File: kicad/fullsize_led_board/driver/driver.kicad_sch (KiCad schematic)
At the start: 131 parts, among them J4 Anodes Header, J5 Cathodes Header, Q1 SQ2351CES, Q10 SQ2351CES, Q11 SQ2351CES, Q12 SQ2351CES, Q13 SQ2351CES, Q14 SQ2351CES, Q15 SQ2351CES, Q16 SQ2351CES, Q17 SQ2351CES, Q18 SQ2351CES, Q19 SQ2351CES, Q2 SQ2351CES, Q20 SQ2351CES, Q21 SQ2351CES, Q22 SQ2351CES, Q23 SQ2351CES, Q24 SQ2351CES, Q3 SQ2351CES, Q4 SQ2351CES, Q5 SQ2351CES, Q6 SQ2351CES, Q7 SQ2351CES, Q8 SQ2351CES, Q9 SQ2351CES, U1 74HCT541, U2 74HCT595, U3 74HCT595, U4 74HCT595, U5 TPIC6B595N, U6 TPIC6B595N, U7 TPIC6B595N, U8 TPIC6B595N

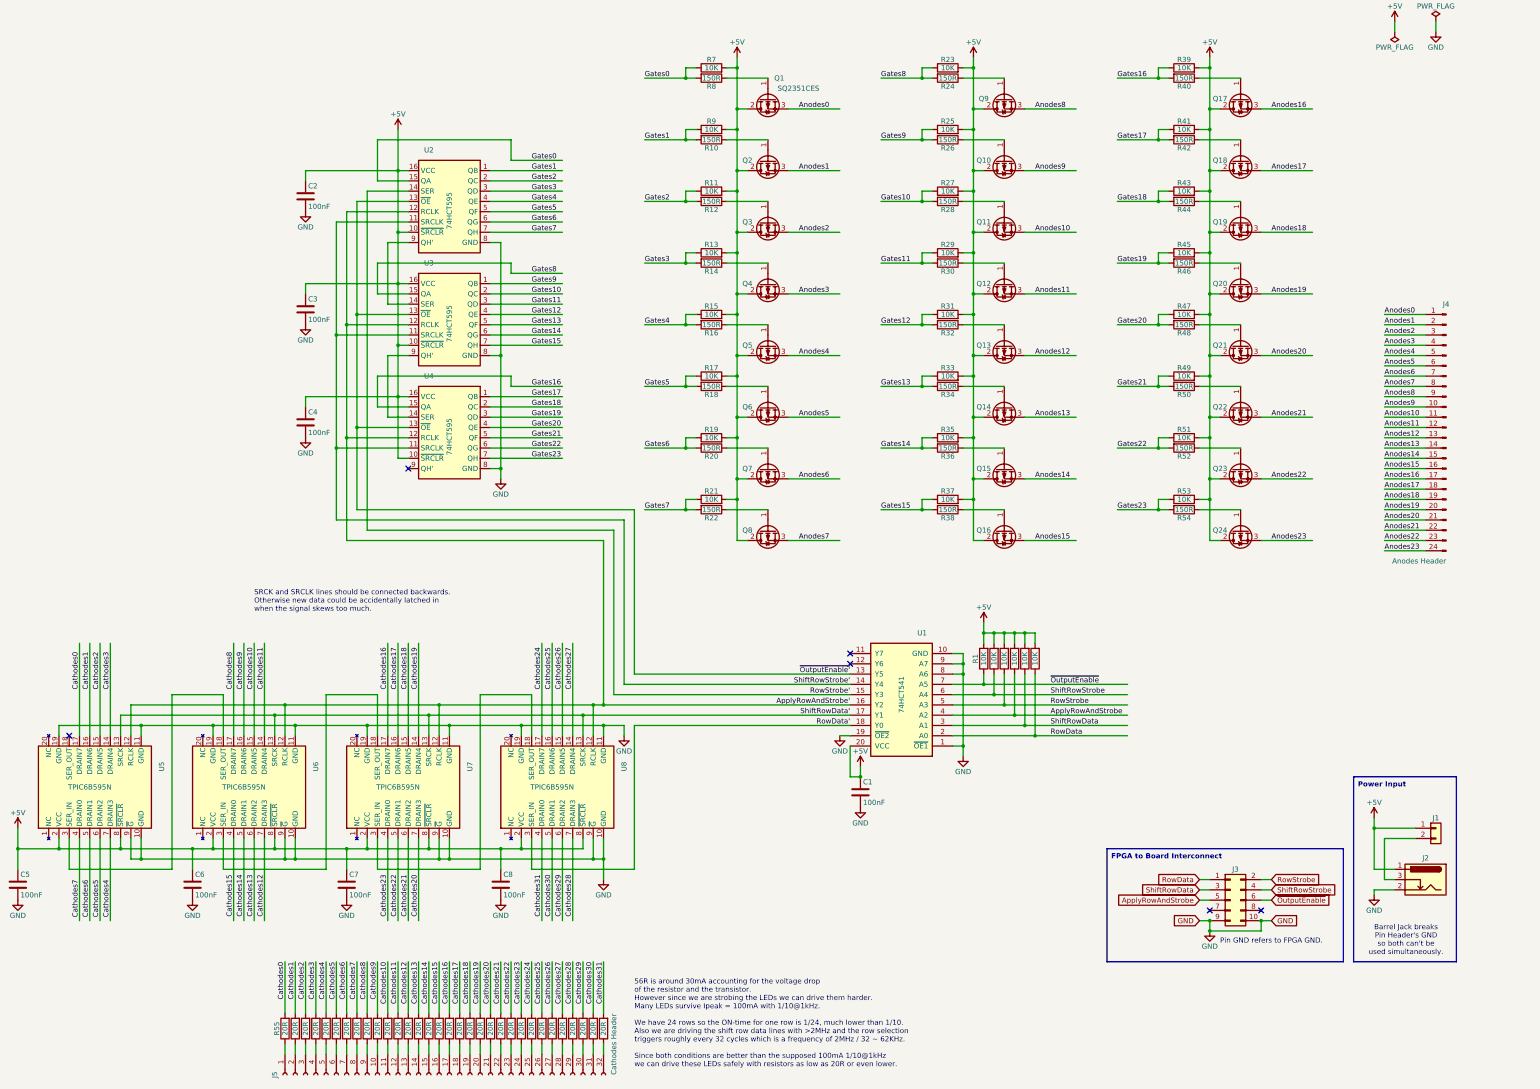
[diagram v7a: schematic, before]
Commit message: kicad: wip migrating to kicad 9.0, fullsize board done
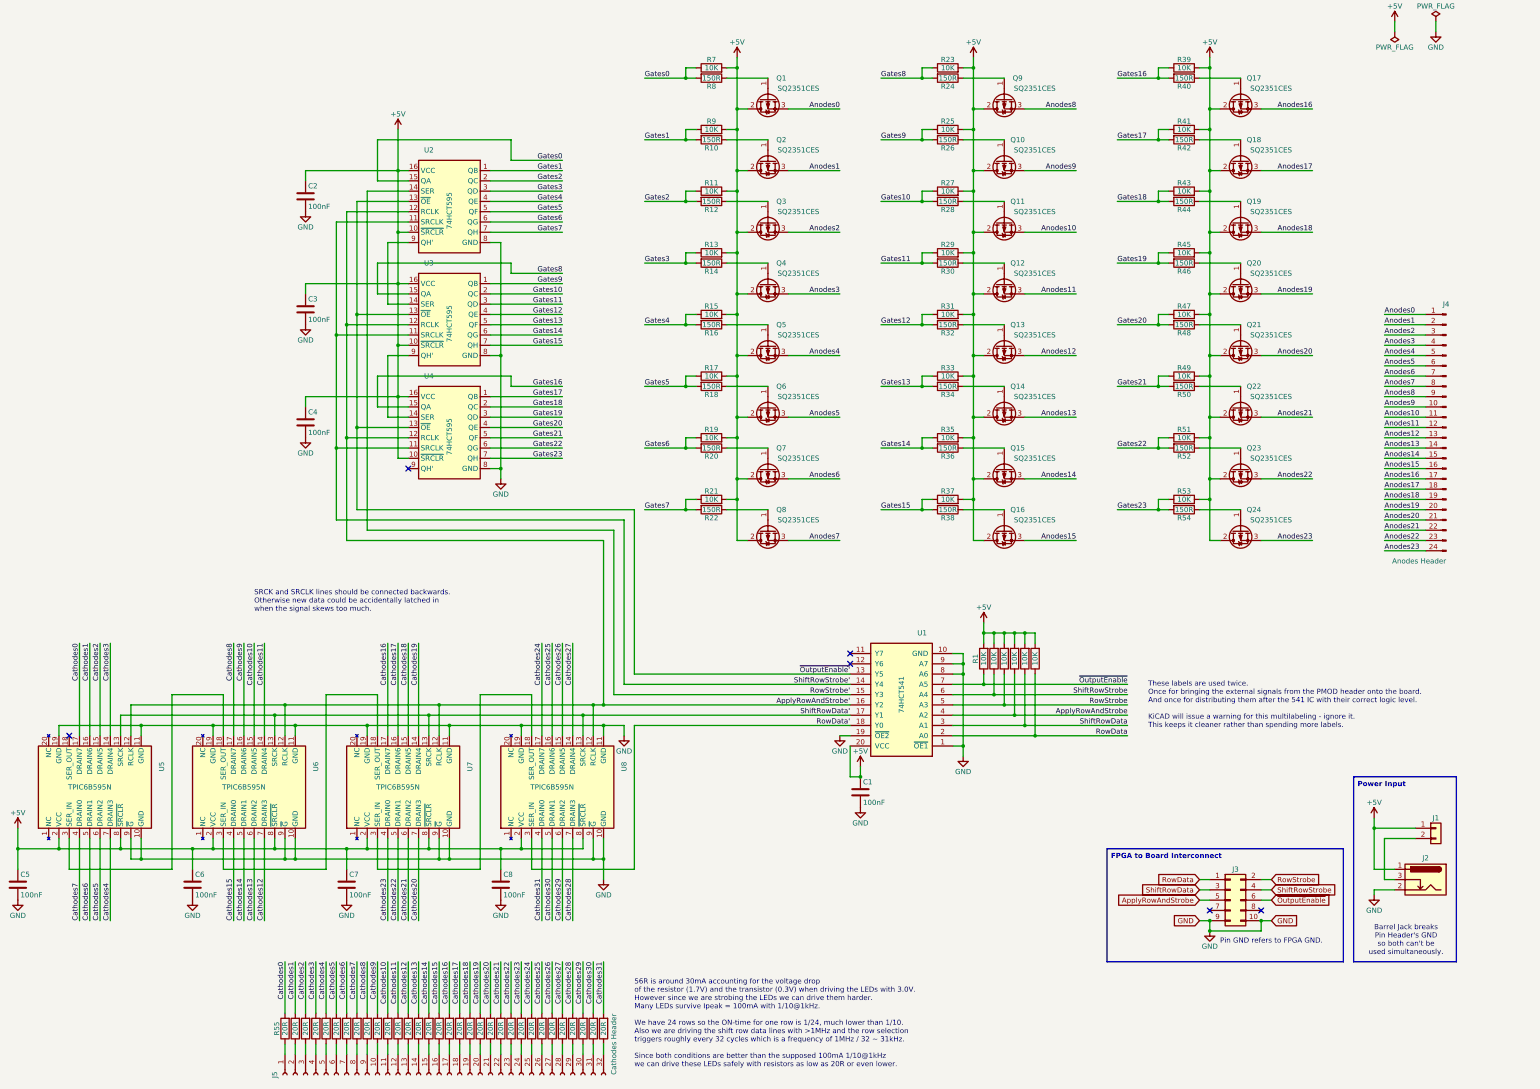
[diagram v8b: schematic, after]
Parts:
- removed Q1, Q10, Q11, Q12, Q13, Q14, Q15, Q16, Q17, Q18, Q19, Q2, Q20, Q21, Q22, Q23, Q24, Q3, Q4, Q5, Q6, Q7, Q8, Q9: SQ2351CES, Package_TO_SOT_SMD:SOT-23-3, symbol Transistor_FET:IRF4905
- removed U1: 74HCT541, Package_DIP:DIP-20_W7.62mm, symbol 74xx:74AHCT541
- removed U2, U3, U4: 74HCT595, Package_SO:SOIC-16_3.9x9.9mm_P1.27mm, symbol 74xx:74HCT595
- removed U5, U6, U7, U8: TPIC6B595N, Package_DIP:DIP-20_W7.62mm, symbol Interface_Expansion:TPIC6595
- added Q1, Q10, Q11, Q12, Q13, Q14, Q15, Q16, Q17, Q18, Q19, Q2, Q20, Q21, Q22, Q23, Q24, Q3, Q4, Q5, Q6, Q7, Q8, Q9: SQ2351CES, Package_TO_SOT_SMD:SOT-23-3, symbol symbol_library:SQ2351CES
- added U1: 74HCT541, Package_DIP:DIP-20_W7.62mm, symbol symbol_library:74HCT541
- added U2, U3, U4: 74HCT595, Package_SO:SOIC-16_3.9x9.9mm_P1.27mm, symbol symbol_library:74HCT595
- added U5, U6, U7, U8: TPIC6B595N, Package_DIP:DIP-20_W7.62mm, symbol symbol_library:TPIC6B595N
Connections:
- net +5V: now also Q1.2 (S), Q10.2 (S), Q11.2 (S), Q12.2 (S), Q13.2 (S), Q14.2 (S), Q15.2 (S), Q16.2 (S), Q17.2 (S), Q18.2 (S), Q19.2 (S), Q2.2 (S), Q20.2 (S), Q21.2 (S), Q22.2 (S), Q23.2 (S), Q24.2 (S), Q3.2 (S), Q4.2 (S), Q5.2 (S), Q6.2 (S), Q7.2 (S), Q8.2 (S), Q9.2 (S), U1.20 (VCC), U2.10 (~{SRCLR}), U2.16 (VCC), U3.10 (~{SRCLR}), U3.16 (VCC), U4.10 (~{SRCLR}), U4.16 (VCC), U5.2 (VCC), U5.8 (~{SRCLR}), U6.2 (VCC), U6.8 (~{SRCLR}), U7.2 (VCC), U7.8 (~{SRCLR}), U8.2 (VCC), U8.8 (~{SRCLR})
- net Anodes0: now also Q1.3 (D)
- net Anodes1: now also Q2.3 (D)
- net Anodes10: now also Q11.3 (D)
- net Anodes11: now also Q12.3 (D)
- net Anodes12: now also Q13.3 (D)
- net Anodes13: now also Q14.3 (D)
- net Anodes14: now also Q15.3 (D)
- net Anodes15: now also Q16.3 (D)
- net Anodes16: now also Q17.3 (D)
- net Anodes17: now also Q18.3 (D)
- net Anodes18: now also Q19.3 (D)
- net Anodes19: now also Q20.3 (D)
- net Anodes2: now also Q3.3 (D)
- net Anodes20: now also Q21.3 (D)
- net Anodes21: now also Q22.3 (D)
- net Anodes22: now also Q23.3 (D)
- net Anodes23: now also Q24.3 (D)
- net Anodes3: now also Q4.3 (D)
- net Anodes4: now also Q5.3 (D)
- net Anodes5: now also Q6.3 (D)
- net Anodes6: now also Q7.3 (D)
- net Anodes7: now also Q8.3 (D)
- net Anodes8: now also Q9.3 (D)
- net Anodes9: now also Q10.3 (D)
- net ApplyRowAndStrobe: now also U1.4 (A2)
- net ApplyRowAndStrobe': now also U1.16 (Y2), U2.12 (RCLK), U3.12 (RCLK), U4.12 (RCLK), U5.12 (RCLK), U6.12 (RCLK), U7.12 (RCLK), U8.12 (RCLK)
- net Cathodes0: now also U5.17 (DRAIN7)
- net Cathodes1: now also U5.16 (DRAIN6)
- net Cathodes10: now also U6.15 (DRAIN5)
- net Cathodes11: now also U6.14 (DRAIN4)
- net Cathodes12: now also U6.7 (DRAIN3)
- net Cathodes13: now also U6.6 (DRAIN2)
- net Cathodes14: now also U6.5 (DRAIN1)
- net Cathodes15: now also U6.4 (DRAIN0)
- net Cathodes16: now also U7.17 (DRAIN7)
- net Cathodes17: now also U7.16 (DRAIN6)
- net Cathodes18: now also U7.15 (DRAIN5)
- net Cathodes19: now also U7.14 (DRAIN4)
- net Cathodes2: now also U5.15 (DRAIN5)
- net Cathodes20: now also U7.7 (DRAIN3)
- net Cathodes21: now also U7.6 (DRAIN2)
- net Cathodes22: now also U7.5 (DRAIN1)
- net Cathodes23: now also U7.4 (DRAIN0)
- net Cathodes24: now also U8.17 (DRAIN7)
- net Cathodes25: now also U8.16 (DRAIN6)
- net Cathodes26: now also U8.15 (DRAIN5)
- net Cathodes27: now also U8.14 (DRAIN4)
- net Cathodes28: now also U8.7 (DRAIN3)
- net Cathodes29: now also U8.6 (DRAIN2)
- net Cathodes3: now also U5.14 (DRAIN4)
- net Cathodes30: now also U8.5 (DRAIN1)
- net Cathodes31: now also U8.4 (DRAIN0)
- net Cathodes4: now also U5.7 (DRAIN3)
- net Cathodes5: now also U5.6 (DRAIN2)
- net Cathodes6: now also U5.5 (DRAIN1)
- net Cathodes7: now also U5.4 (DRAIN0)
- net Cathodes8: now also U6.17 (DRAIN7)
- net Cathodes9: now also U6.16 (DRAIN6)
- net GND: now also U1.1 (~{OE1}), U1.10 (GND), U1.19 (~{OE2}), U1.8 (A6), U1.9 (A7), U2.8 (GND), U3.8 (GND), U4.8 (GND), U5.10 (GND), U5.11 (GND), U5.19 (GND), U5.9 (~{G}), U6.10 (GND), U6.11 (GND), U6.19 (GND), U6.9 (~{G}), U7.10 (GND), U7.11 (GND), U7.19 (GND), U7.9 (~{G}), U8.10 (GND), U8.11 (GND), U8.19 (GND), U8.9 (~{G})
- net Gates0: now also U2.15 (QA)
- net Gates1: now also U2.1 (QB)
- net Gates10: now also U3.2 (QC)
- net Gates11: now also U3.3 (QD)
- net Gates12: now also U3.4 (QE)
- net Gates13: now also U3.5 (QF)
- net Gates14: now also U3.6 (QG)
- net Gates15: now also U3.7 (QH)
- net Gates16: now also U4.15 (QA)
- net Gates17: now also U4.1 (QB)
- net Gates18: now also U4.2 (QC)
- net Gates19: now also U4.3 (QD)
- net Gates2: now also U2.2 (QC)
- net Gates20: now also U4.4 (QE)
- net Gates21: now also U4.5 (QF)
- net Gates22: now also U4.6 (QG)
- net Gates23: now also U4.7 (QH)
- net Gates3: now also U2.3 (QD)
- net Gates4: now also U2.4 (QE)
- net Gates5: now also U2.5 (QF)
- net Gates6: now also U2.6 (QG)
- net Gates7: now also U2.7 (QH)
- net Gates8: now also U3.15 (QA)
- net Gates9: now also U3.1 (QB)
- net RowData: now also U1.2 (A0)
- net RowData': now also U1.18 (Y0), U8.3 (SER_IN)
- net RowStrobe: now also U1.5 (A3)
- net RowStrobe': now also U1.15 (Y3), U2.14 (SER)
- net ShiftRowData: now also U1.3 (A1)
- net ShiftRowData': now also U1.17 (Y1), U5.13 (SRCK), U6.13 (SRCK), U7.13 (SRCK), U8.13 (SRCK)
- net ShiftRowStrobe: now also U1.6 (A4)
- net ShiftRowStrobe': now also U1.14 (Y4), U2.11 (SRCLK), U3.11 (SRCLK), U4.11 (SRCLK)
- net ~{OutputEnable'}: now also U1.13 (Y5), U2.13 (~{OE}), U3.13 (~{OE}), U4.13 (~{OE})
- net ~{OutputEnable}: now also U1.7 (A5)
- net at R26.1: now also Q10.1 (G)
- net at R48.1: now also Q21.1 (G)
- net at R50.1: now also Q22.1 (G)
- net at R32.1: now also Q13.1 (G)
- net at R12.1: now also Q3.1 (G)
- net at R46.1: now also Q20.1 (G)
- net at R34.1: now also Q14.1 (G)
- net at R40.1: now also Q17.1 (G)
- net at R30.1: now also Q12.1 (G)
- net at R42.1: now also Q18.1 (G)
- net at R36.1: now also Q15.1 (G)
- net at R20.1: now also Q7.1 (G)
- net at R8.1: now also Q1.1 (G)
- net at R38.1: now also Q16.1 (G)
- net at R28.1: now also Q11.1 (G)
- net at R14.1: now also Q4.1 (G)
- net at R52.1: now also Q23.1 (G)
- net at R22.1: now also Q8.1 (G)
- net at R10.1: now also Q2.1 (G)
- net at R54.1: now also Q24.1 (G)
- net at R18.1: now also Q6.1 (G)
- net at R44.1: now also Q19.1 (G)
- net at R16.1: now also Q5.1 (G)
- net at R24.1: now also Q9.1 (G)
- new net: U3.9 (QH'), U4.14 (SER)
- new net: U7.3 (SER_IN), U8.18 (SER_OUT)
- new net: U5.3 (SER_IN), U6.18 (SER_OUT)
- new net: U2.9 (QH'), U3.14 (SER)
- new net: U6.3 (SER_IN), U7.18 (SER_OUT)
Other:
- note added: "56R is around 30mA accounting for the voltage drop of the resistor (1.7V) and the transistor (0.3V) when driving the LEDs with 3.0V. However since we are strobing the LEDs we can drive them harder. Many LEDs survive Ipeak = 100mA with 1/10@1kHz. We have 24 rows so the ON-time for one row is 1/24, much lower than 1/10. Also we are driving the shift row data lines with >1MHz and the row selection t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"
- note added: "These labels are used twice. Once for bringing the external signals from the PMOD header onto the board. And once for distributing them after the 541 IC with their correct logic level. KiCAD will issue a warning for this multilabeling - ignore it. This keeps it cleaner rather than spending more labels."
- note removed: "56R is around 30mA accounting for the voltage drop of the resistor and the transistor. However since we are strobing the LEDs we can drive them harder. Many LEDs survive Ipeak = 100mA with 1/10@1kHz. We have 24 rows so the ON-time for one row is 1/24, much lower than 1/10. Also we are driving the shift row data lines with >2MHz and the row selection triggers roughly every 32 cycles which is a fre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"
